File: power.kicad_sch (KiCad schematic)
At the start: 26 parts, among them U10 DS4432U+, U11 RT9080-33GJ5, U5 MCP1824T-1802E, U6 MCP1824T-0802E, U8 INA260, U9 SIC431AED-T1-GE3

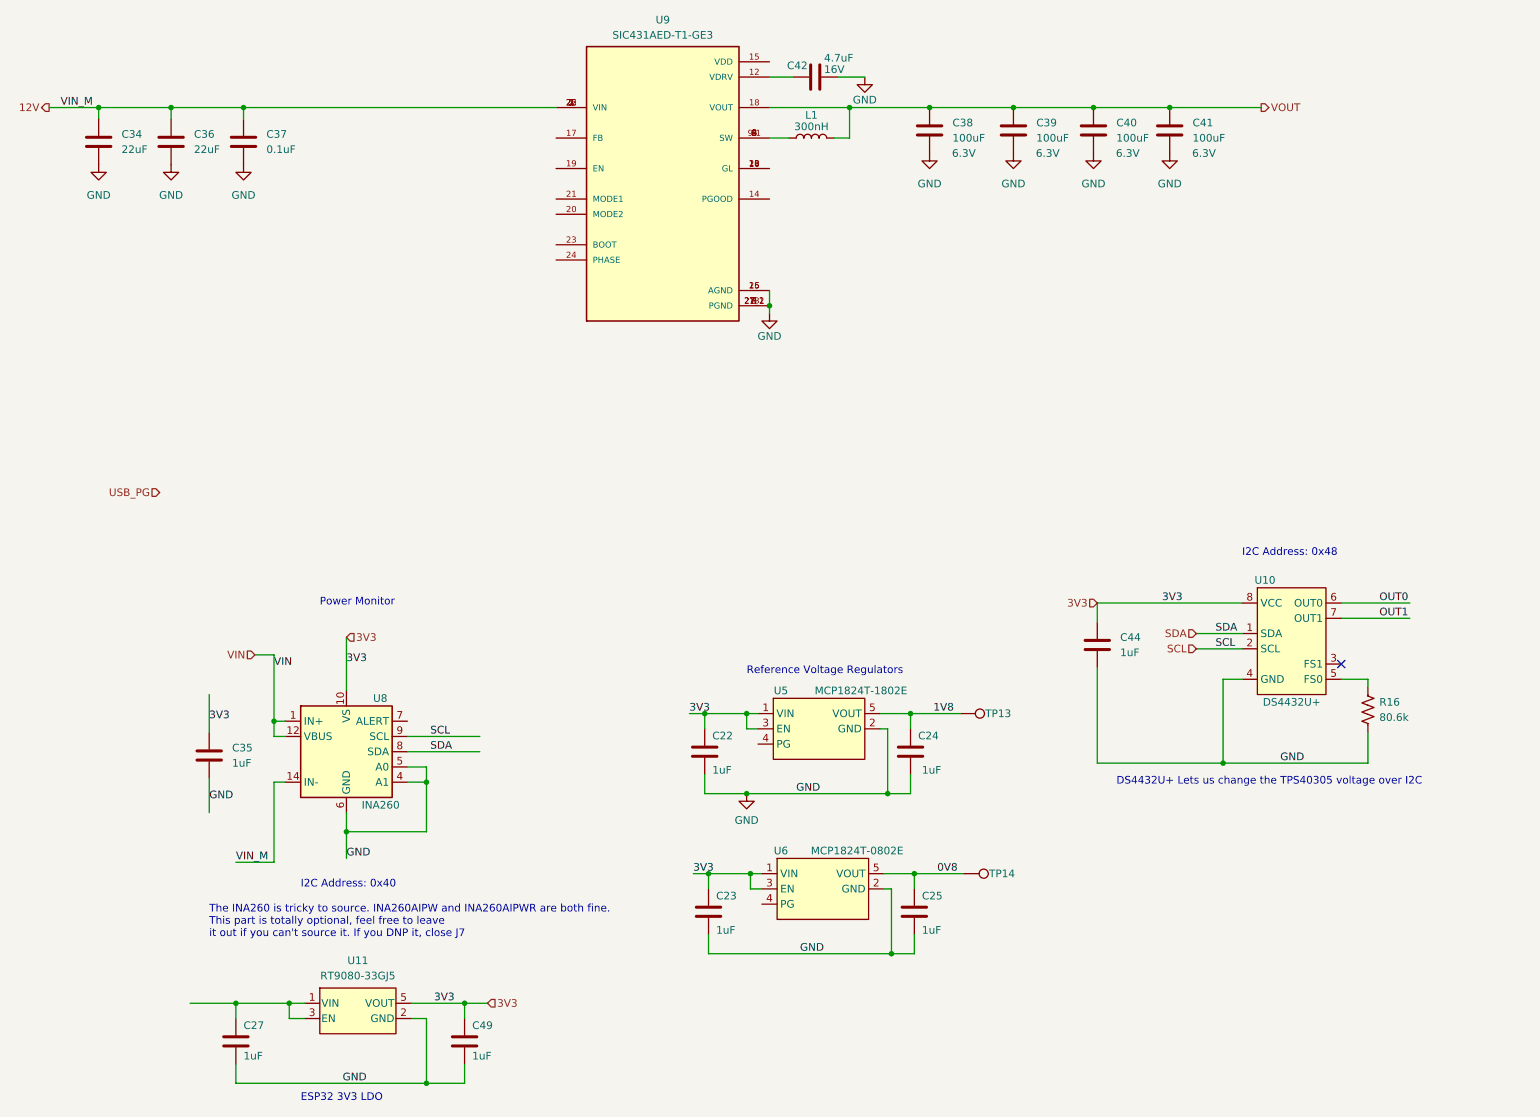
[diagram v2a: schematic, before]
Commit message: SCH Draft 3, PCB Start
Finished some last minute changes to change 1V8 to 1V2 based on discord feedback. Updated level shifter and moved 25MHz oscillator to use 3V3 and be shifted down. Started working on layout.
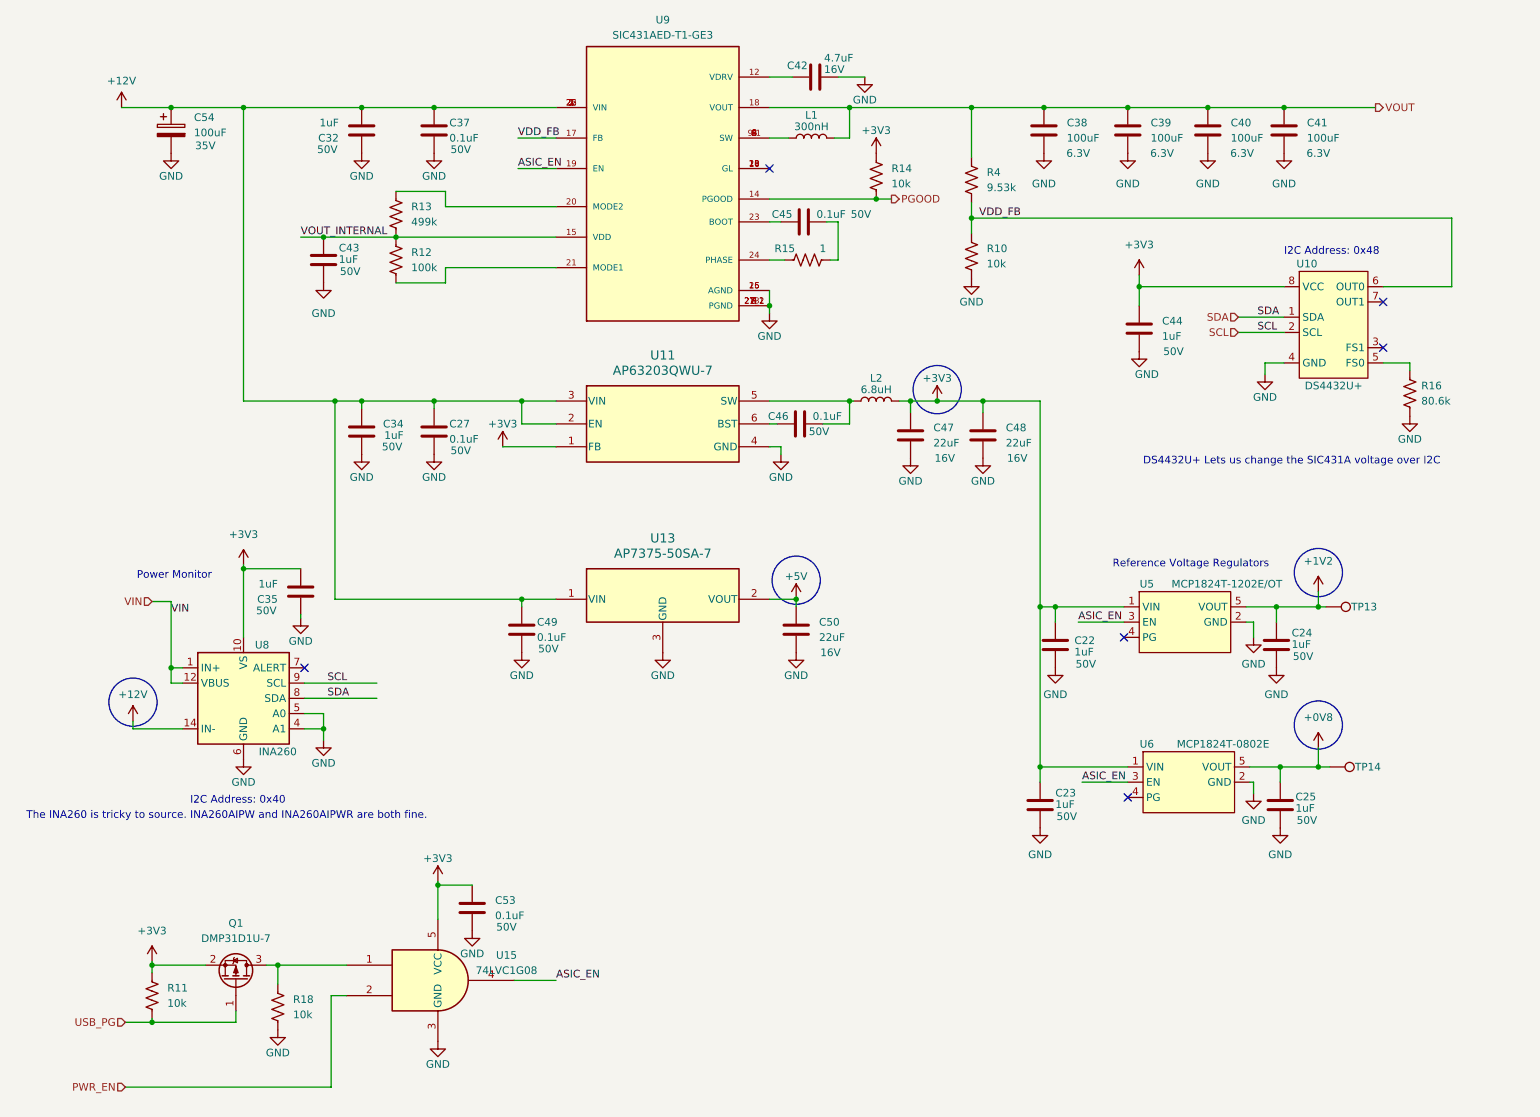
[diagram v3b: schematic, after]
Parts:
- removed C36: 22uF, Capacitor_SMD:C_1210_3225Metric, symbol Device:C
- removed U11: RT9080-33GJ5, bitaxe:RT9080-33GJ5, symbol bitaxe:RT9080-33GJ5
- added C32, C43: 1uF, Capacitor_SMD:C_0603_1608Metric, symbol Device:C
- added C45, C46, C53: 0.1uF, Capacitor_SMD:C_0402_1005Metric, symbol Device:C
- added C47, C48, C50: 22uF, Capacitor_SMD:C_0805_2012Metric, symbol Device:C
- added C54: 100uF, bitaxe:CAP_WCAP-ASLI_06p3X07p7_WRE, symbol Device:C_Polarized
- added L2: 6.8uH, bitaxe:IND_VLS5045EX-100M, symbol Device:L
- added Q1: DMP31D1U-7, bitaxe:DIODESINC_SOT-23, symbol Device:Q_PMOS_GSD
- added R10, R11, R14, R18: 10k, Resistor_SMD:R_0402_1005Metric, symbol Device:R_US
- added R12: 100k, Resistor_SMD:R_0402_1005Metric, symbol Device:R_US
- added R13: 499k, Resistor_SMD:R_0402_1005Metric, symbol Device:R_US
- added R15: 1, Resistor_SMD:R_0402_1005Metric, symbol Device:R_US
- added R4: 9.53k, Resistor_SMD:R_0402_1005Metric, symbol Device:R_US
- added U11: AP63203QWU-7, bitaxe:TSOT26_DIO, symbol bitaxe:AP63203QWU-7
- added U13: AP7375-50SA-7, bitaxe:DIODESINC_SOT-23, symbol bitaxe:AP7375-50SA-7
- added U15: 74LVC1G08, Package_TO_SOT_SMD:SOT-353_SC-70-5, symbol 74xGxx:74LVC1G08
- C22, C23, C24, C25, C35, C44: footprint Capacitor_SMD:C_0402_1005Metric -> Capacitor_SMD:C_0603_1608Metric; DK 587-5514-1-ND -> 311-2082-1-ND; PARTNO EMK105BJ105MV-F -> CC0603KRX7R9BB105; Voltage (none) -> 50V
- C27, C49: value 1uF -> 0.1uF; DK 587-5514-1-ND -> 490-13342-1-ND; PARTNO EMK105BJ105MV-F -> GRM155R71H104KE14J; Voltage (none) -> 50V
- C34: value 22uF -> 1uF; footprint Capacitor_SMD:C_1210_3225Metric -> Capacitor_SMD:C_0603_1608Metric; DK 1276-3392-1-ND -> 311-2082-1-ND; PARTNO CL32B226KAJNNNE -> CC0603KRX7R9BB105; Voltage (none) -> 50V
- C37: DK 1276-6720-1-ND -> 490-13342-1-ND; PARTNO CL05B104KA5NNNC -> GRM155R71H104KE14J; Voltage (none) -> 50V
- L1: DK (none) -> 118-SPB1007-R30MCT-ND; PARTNO (none) -> SPB1007-R30M
- U5: value MCP1824T-1802E -> MCP1824T-1202E/OT; DK MCP1824T-1802E/OTCT-ND -> MCP1824T-1202E/OTCT-ND; PARTNO MCP1824T-1802E/OT -> MCP1824T-1202E/OT
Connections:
- net OUT0 is gone; now on net VDD_FB: U10.6 (OUT0)
- net GND: now also C34.1, C35.1, C32.1, C43.2, C47.2, C48.2, C50.2, C53.2, C54.2, R10.2, R18.2, U11.4 (GND), U13.3 (GND), U15.3 (GND); no longer C34.2, C35.2
- net USB_PG: now also Q1.1 (G), R11.2
- net VOUT: now also R4.1
- net +12V: now reaches C27.1
- net +12V: now also C34.2, C37.1, C49.1, U8.14 (IN-), U8.15 (IN-), U8.16 (IN-), U9.1 (VIN), U9.2 (VIN), U9.22 (VIN), U9.26 (VIN), C32.2, C54.1, U11.2 (EN), U11.3 (VIN), U13.1 (VIN)
- net PGOOD: now reaches U9.14 (PGOOD)
- net PGOOD: now also R14.2
- net VOUT_INTERNAL: now reaches U9.15 (VDD)
- net VOUT_INTERNAL: now also C43.1, R12.1, R13.2
- net VDD_FB: now reaches U9.17 (FB)
- net VDD_FB: now also R10.1, R4.2
- net ASIC_EN: now reaches U9.19 (EN)
- net ASIC_EN: now also U5.3 (EN), U6.3 (EN), U15.4
- net at U9.20 (MODE2): now also R13.1
- net at U9.21 (MODE1): now also R12.2
- net at U9.23 (BOOT): now also C45.1
- net at U9.24 (PHASE): now also R15.1
- net 0V8 renamed +0V8
- removed net 12V: C34.1, C37.1, U8.14 (IN-), U8.15 (IN-), U8.16 (IN-), U9.1 (VIN), U9.2 (VIN), U9.22 (VIN), U9.26 (VIN)
- net 1V8 renamed +1V2
- net 3V3 renamed +3V3
- net +3V3: now also C35.2, C47.1, C48.1, C53.1, L2.2, Q1.2 (S), R11.1, R14.1, U11.1 (FB), U15.5 (VCC); no longer C35.1, C49.1, U5.3 (EN), U6.3 (EN)
- net OUT1: no longer names the net of U10.7 (OUT1)
- net VIN renamed IN+
- new net: C46.1, U11.6 (BST)
- new net: C46.2, L2.1, U11.5 (SW)
- new net: Q1.3 (D), R18.1, U15.1
- new net: C45.2, R15.2
- new net +5V: C50.1, U13.2 (VOUT)
- new net PWR_EN: U15.2
- no-connect marks 1 -> 6
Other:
- note added: "DS4432U+ Lets us change the SIC431A voltage over I2C"
- note added: "The INA260 is tricky to source. INA260AIPW and INA260AIPWR are both fine."
- note removed: "DS4432U+ Lets us change the TPS40305 voltage over I2C"
- note removed: "ESP32 3V3 LDO"
- note removed: "The INA260 is tricky to source. INA260AIPW and INA260AIPWR are both fine. This part is totally optional, feel free to leave it out if you can't source it. If you DNP it, close J7"
- moved on the sheet: C22, C23, C24, C25, C37, C38, C39, C40, C41, C44, R16, TP13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

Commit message: Layout completed for concept 1
Need to still work on vias and fills, move some parts around.
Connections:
- now unconnected: U9.10 (GL), U9.11 (GL), U9.28 (GL)
- no-connect marks 6 -> 8
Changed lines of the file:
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@@
   (junction (at 151.765 77.47) (diameter 0) (color 0 0 0 0)
   )
+  (no_connect (at 138.43 37.465))
   (no_connect (at 240.665 60.96))
   (no_connect (at 60.96 121.92))
   (no_connect (at 198.12 143.51))
   (no_connect (at 240.665 68.58))
+  (no_connect (at 138.43 36.195))
   (no_connect (at 197.485 116.84))
   (no_connect (at 138.43 38.735))
